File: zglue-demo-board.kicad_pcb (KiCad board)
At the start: 6 copper layers, 56 x 66 mm, 151 parts, among them J1 3220-10-0100-00, J10 0473460001, J2 DF13A-2P-1.25H, J3 3220-10-0100-00, J4 2x20_Header_Female, J5 0473460001, J6 556500488, J7 556500488, J8 WE_686115148922, J9 WE_686115148922_FLIPPED, U1 MCP1700T-3302E_TT, U2 NTS0104BQ, U3 NTS0104BQ, U4 NTS0104BQ, U5 93LC56CT-IMC, U6 FT4232HQ, U7 NTB0104BQ, U8 NTB0104BQ, Y1 ASFLMB-12.000MHZ-LC-T

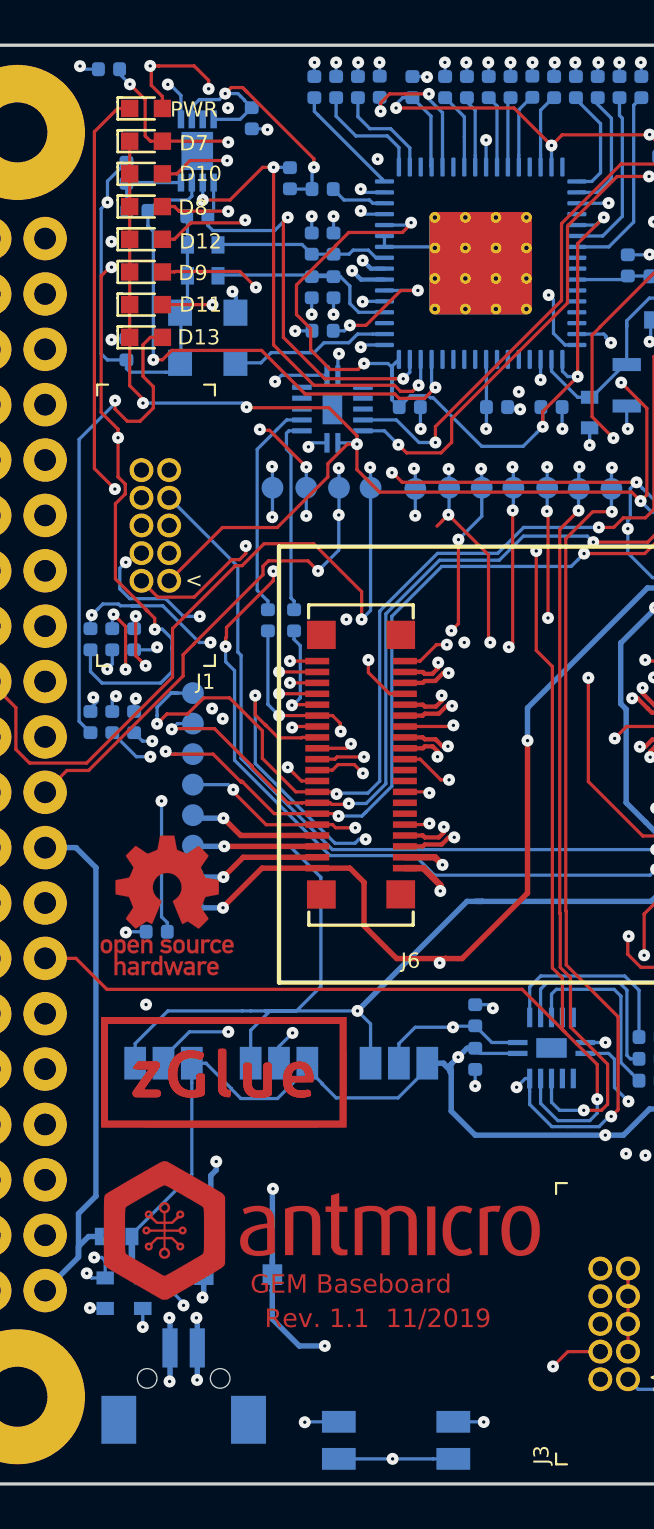
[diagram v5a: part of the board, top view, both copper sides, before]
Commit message: Connected PWR_BTN to VUSB, updated PCB
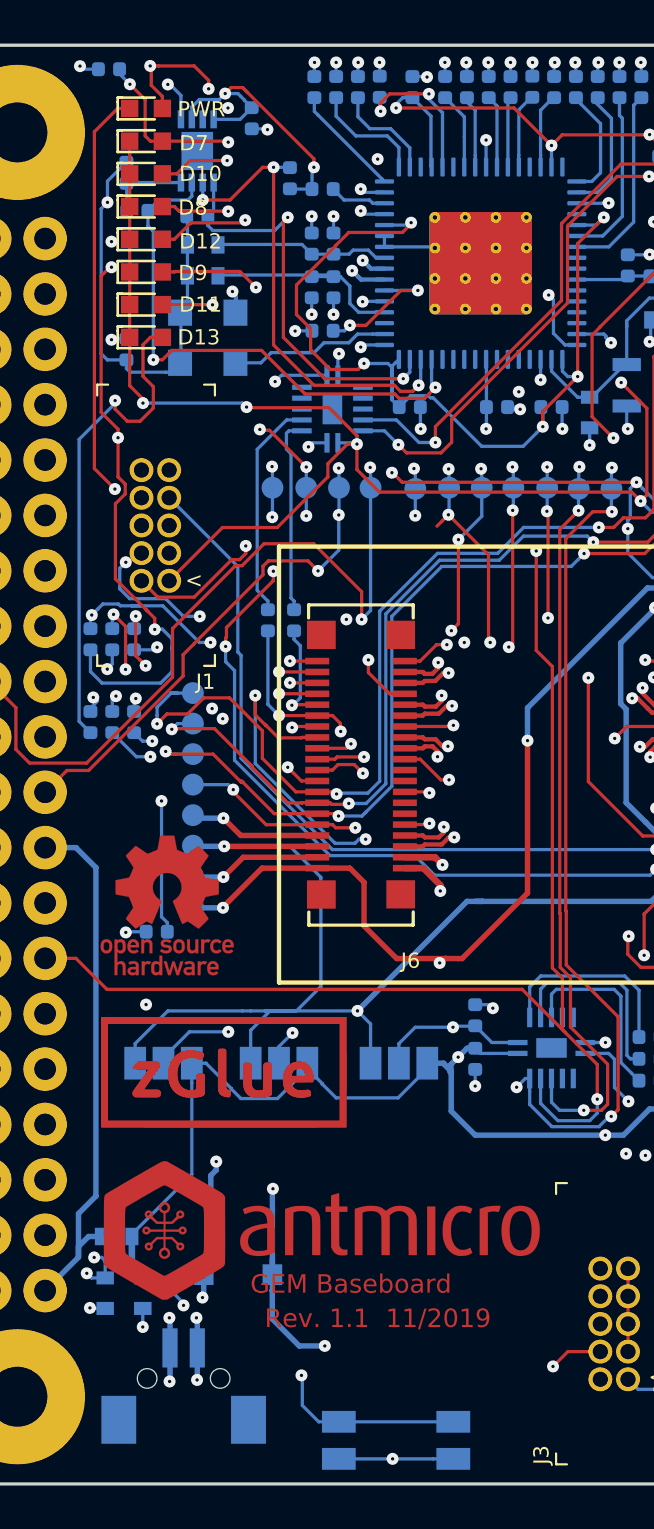
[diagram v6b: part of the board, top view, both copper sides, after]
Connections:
- S1 pad 2: GND -> /VUSB
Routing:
- net /VUSB: track 69.7 -> 78.3 mm, vias 9 -> 10
- net GND: track 183.5 -> 180.6 mm, vias 81 -> 79
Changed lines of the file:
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@@
   (layers
     (0 F.Cu signal)
-    (1 In1.Cu signal hide)
+    (1 In1.Cu signal)
     (2 In2.Cu signal)
     (3 In3.Cu signal)
-    (4 In4.Cu signal hide)
+    (4 In4.Cu signal)
     (31 B.Cu signal)
     (32 B.Adhes user hide)
@@
     (fp_line (start 3.9 3.25) (end -3.9 3.25) (layer B.CrtYd) (width 0.05))
     (pad 2 smd rect (at 2.625 -0.85 180) (size 1.55 1) (layers B.Cu B.Paste B.Mask)
-      (net 2 GND))
+      (net 43 /VUSB))
     (pad 2 smd rect (at -2.625 -0.85 180) (size 1.55 1) (layers B.Cu B.Paste B.Mask)
-      (net 2 GND))
+      (net 43 /VUSB))
     (pad 1 smd rect (at -2.625 0.85 180) (size 1.55 1) (layers B.Cu B.Paste B.Mask)
       (net 101 /PWR_BTN))
@@
     (at 37.2 33.15)
     (attr smd)
-    (fp_text reference PWR (at 2.2 0.05 180) (layer F.SilkS)
+    (fp_text reference PWR (at 2.54 0.04 180) (layer F.SilkS)
       (effects (font (size 0.7 0.7) (thickness 0.15)))
     )
@@
   (segment (start 73.85 57.1) (end 73.970876 56.979124) (width 0.15) (layer B.Cu) (net 2))
   (via (at 73.970876 56.979124) (size 0.55) (drill 0.15) (layers F.Cu B.Cu) (net 2))
-  (segment (start 52.68 93.4) (end 52.69 93.41) (width 0.15) (layer B.Cu) (net 2))
-  (segment (start 51.295 93.4) (end 52.68 93.4) (width 0.15) (layer B.Cu) (net 2))
-  (via (at 52.69 93.41) (size 0.55) (drill 0.15) (layers F.Cu B.Cu) (net 2))
-  (segment (start 44.5 93.4) (end 44.48 93.42) (width 0.15) (layer B.Cu) (net 2))
-  (segment (start 46.045 93.4) (end 44.5 93.4) (width 0.15) (layer B.Cu) (net 2))
-  (via (at 44.48 93.42) (size 0.55) (drill 0.15) (layers F.Cu B.Cu) (net 2))
   (segment (start 59.31 90.18) (end 59.31 86.37) (width 0.15) (layer F.Cu) (net 2))
   (segment (start 74.522078 57.582611) (end 74.522078 56.422078) (width 0.15) (layer In3.Cu) (net 2))
@@
   (via (at 45.4 89.92) (size 0.55) (drill 0.15) (layers F.Cu B.Cu) (net 43))
   (segment (start 44.23 89.92) (end 45.4 89.92) (width 0.25) (layer B.Cu) (net 43))
+  (segment (start 46.045 93.4) (end 51.295 93.4) (width 0.15) (layer B.Cu) (net 43))
+  (segment (start 45.12 93.4) (end 44.37 92.65) (width 0.15) (layer B.Cu) (net 43))
+  (segment (start 46.045 93.4) (end 45.12 93.4) (width 0.15) (layer B.Cu) (net 43))
+  (via (at 44.33 91.27) (size 0.55) (drill 0.15) (layers F.Cu B.Cu) (net 43))
+  (segment (start 44.37 91.31) (end 44.33 91.27) (width 0.15) (layer B.Cu) (net 43))
+  (segment (start 44.37 92.65) (end 44.37 91.31) (width 0.15) (layer B.Cu) (net 43))
   (segment (start 39.845 86.65) (end 39.845 85.885) (width 0.25) (layer B.Cu) (net 44))
   (segment (start 39.845 85.885) (end 40.17 85.56) (width 0.25) (layer B.Cu) (net 44))
